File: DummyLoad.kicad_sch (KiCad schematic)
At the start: 37 parts, among them J1 RF In, J2 RF Out

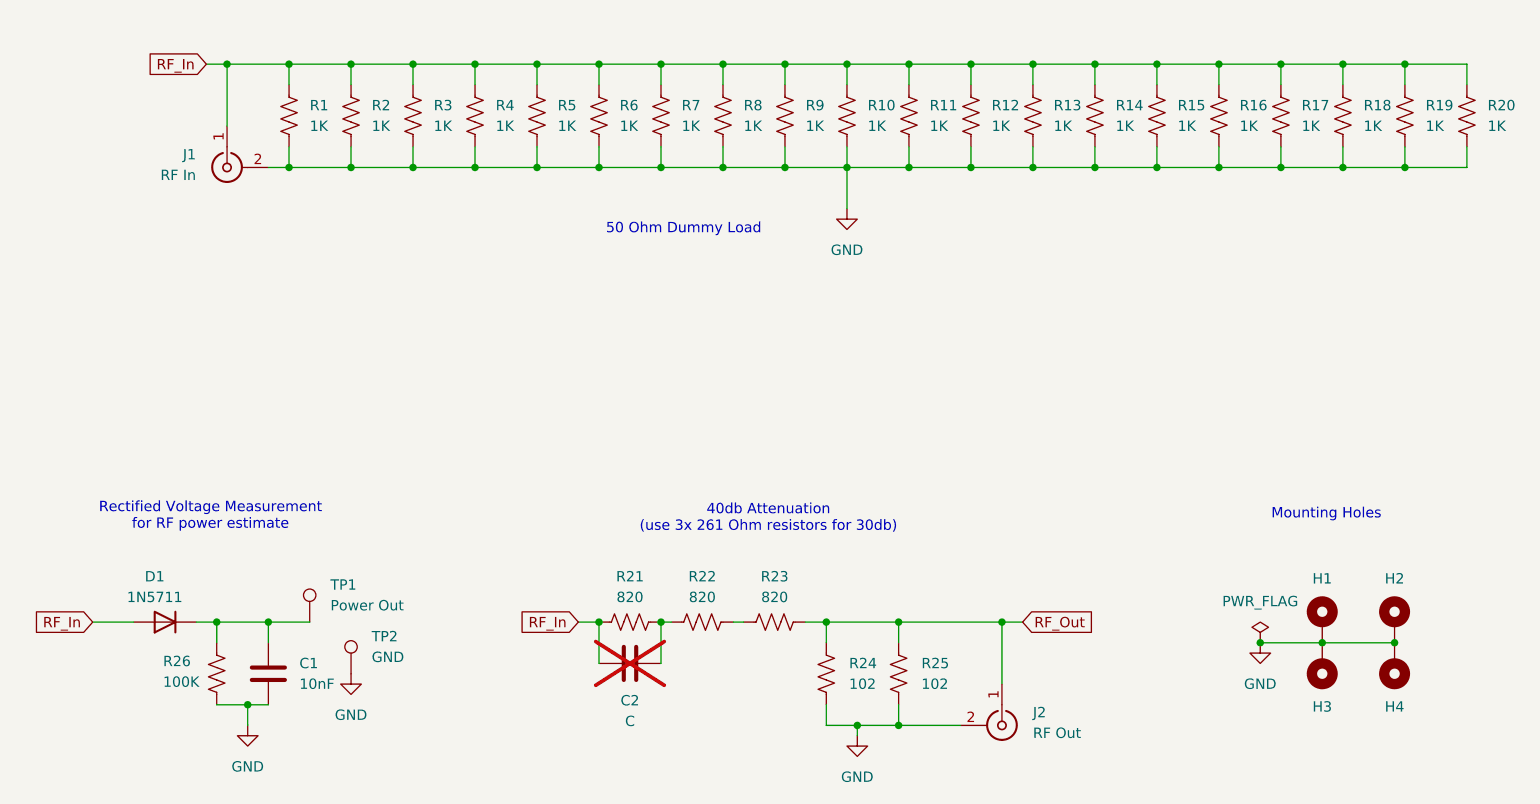
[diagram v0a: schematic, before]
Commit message: Add TH testpoints and update PCB labels/layout
Add two through-hole testpoint footprints (RF In and GND) and reassign existing testpoint references (TP1/TP2 -> TP3/TP4). Adjusted testpoint coordinates and nets, updated multiple silkscreen texts (board name to "50Ω QRP Dummy Load", added designer credit, RF In/Ground labels) and repositioned several text items. Many via coordinates and UUIDs were updated to reflect the layout changes. These edits update the PCB to expose test points and tidy the board silk/placement for assembly and testing.
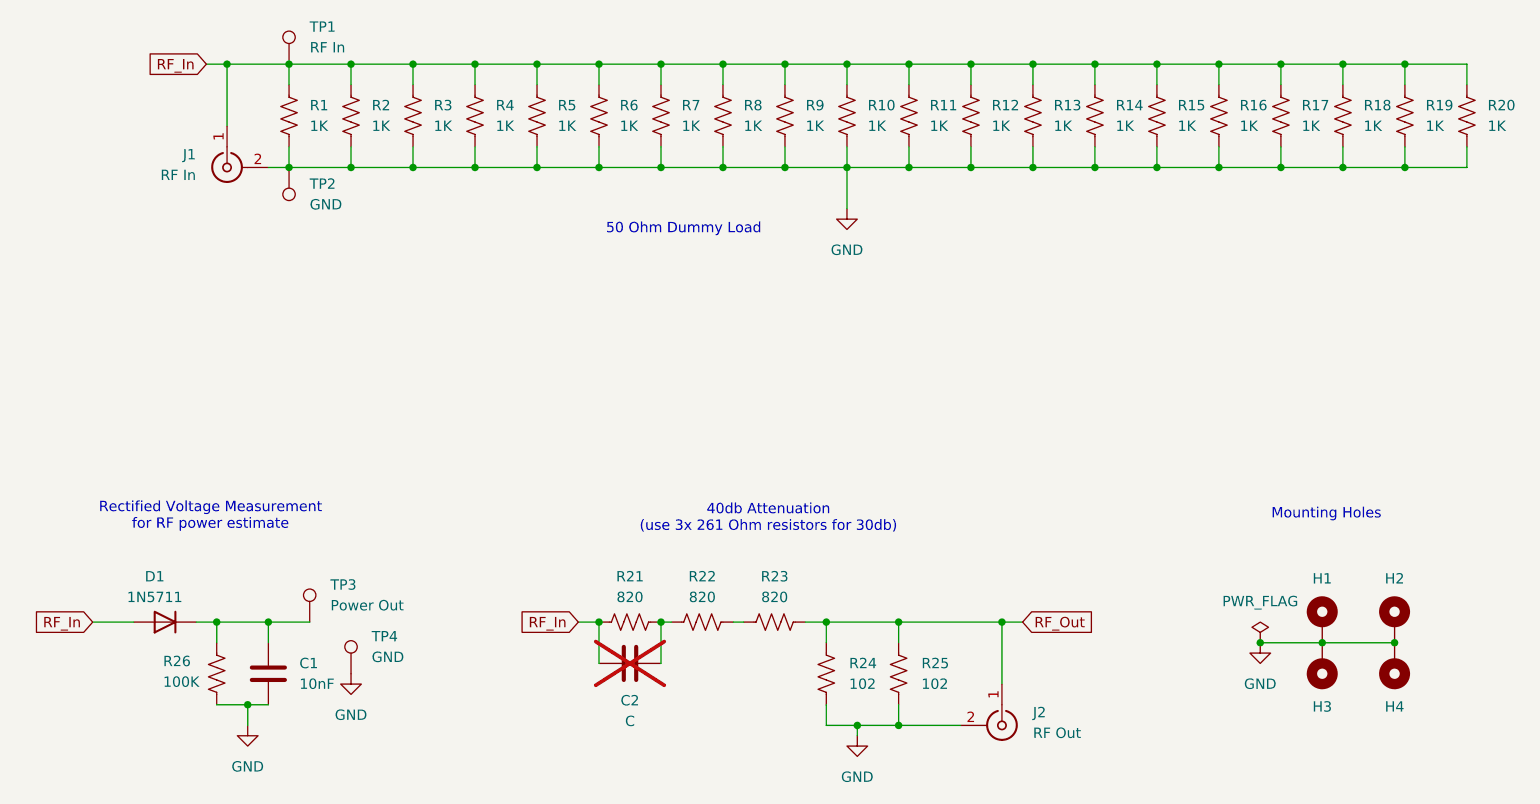
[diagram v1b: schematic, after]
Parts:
- added TP1: RF In, TestPoint:TestPoint_THTPad_D3.0mm_Drill1.5mm, symbol Connector:TestPoint
- added TP2: GND, TestPoint:TestPoint_THTPad_D3.0mm_Drill1.5mm, symbol Connector:TestPoint
- renumbered TP1 to TP3, TP2 to TP4
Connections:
- net GND: now also TP2.1
- net RF_In: now also TP1.1
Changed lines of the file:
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@@
 		(dnp no)
 		(fields_autoplaced yes)
-		(property "Reference" "TP2"
+		(property "Reference" "TP4"
 			(at 88.9 122.4279 0)
 			(effects
@@
 			(project ""
 				(path "/8955e49b-c499-4a31-89c9-ad9bd8b95ad7"
-					(reference "TP2")
+					(reference "TP4")
 					(unit 1)
 				)
@@
 	)
 	(symbol
+		(lib_id "Connector:TestPoint")
+		(at 78.74 64.77 180)
+		(unit 1)
+		(exclude_from_sim no)
+		(in_bom yes)
+		(on_board yes)
+		(dnp no)
+		(fields_autoplaced yes)
+		(property "Reference" "TP2"
+			(at 81.28 66.8019 0)
+			(effects
+				(font
+					(size 1.27 1.27)
+				)
+				(justify right)
+			)
+		)
+		(property "Value" "GND"
+			(at 81.28 69.3419 0)
+			(effects
+				(font
+					(size 1.27 1.27)
+				)
+				(justify right)
+			)
+		)
+		(property "Footprint" "TestPoint:TestPoint_THTPad_D3.0mm_Drill1.5mm"
+			(at 73.66 64.77 0)
+			(effects
+				(font
+					(size 1.27 1.27)
+				)
+				(hide yes)
+			)
+		)
+		(property "Datasheet" "~"
+			(at 73.66 64.77 0)
+			(effects
+				(font
+					(size 1.27 1.27)
+				)
+				(hide yes)
+			)
+		)
+		(property "Description" "test point"
+			(at 78.74 64.77 0)
+			(effects
+				(font
+					(size 1.27 1.27)
+				)
+				(hide yes)
+			)
+		)
+		(pin "1"
+		)
+		(instances
+			(project ""
+				(path "/8955e49b-c499-4a31-89c9-ad9bd8b95ad7"
+					(reference "TP2")
+					(unit 1)
+				)
+			)
+		)
+	)
+	(symbol
 		(lib_id "Device:R_US")
 		(at 185.42 58.42 0)
@@
 	)
 	(symbol
+		(lib_id "Connector:TestPoint")
+		(at 78.74 52.07 0)
+		(unit 1)
+		(exclude_from_sim no)
+		(in_bom yes)
+		(on_board yes)
+		(dnp no)
+		(fields_autoplaced yes)
+		(property "Reference" "TP1"
+			(at 81.28 47.4979 0)
+			(effects
+				(font
+					(size 1.27 1.27)
+				)
+				(justify left)
+			)
+		)
+		(property "Value" "RF In"
+			(at 81.28 50.0379 0)
+			(effects
+				(font
+					(size 1.27 1.27)
+				)
+				(justify left)
+			)
+		)
+		(property "Footprint" "TestPoint:TestPoint_THTPad_D3.0mm_Drill1.5mm"
+			(at 83.82 52.07 0)
+			(effects
+				(font
+					(size 1.27 1.27)
+				)
+				(hide yes)
+			)
+		)
+		(property "Datasheet" "~"
+			(at 83.82 52.07 0)
+			(effects
+				(font
+					(size 1.27 1.27)
+				)
+				(hide yes)
+			)
+		)
+		(property "Description" "test point"
+			(at 78.74 52.07 0)
+			(effects
+				(font
+					(size 1.27 1.27)
+				)
+				(hide yes)
+			)
+		)
+		(pin "1"
+		)
+		(instances
+			(project ""
+				(path "/8955e49b-c499-4a31-89c9-ad9bd8b95ad7"
+					(reference "TP1")
+					(unit 1)
+				)
+			)
+		)
+	)
+	(symbol
 		(lib_id "Device:D")
 		(at 63.5 120.65 180)
@@
 		(dnp no)
 		(fields_autoplaced yes)
-		(property "Reference" "TP1"
+		(property "Reference" "TP3"
 			(at 83.82 116.0779 0)
 			(effects
@@
 			(project ""
 				(path "/8955e49b-c499-4a31-89c9-ad9bd8b95ad7"
-					(reference "TP1")
-					(unit 1)
-				)
+					(reference "TP3")
+					(unit 1)
+				)
